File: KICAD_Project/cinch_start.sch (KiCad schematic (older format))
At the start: 30 parts, among them P101 CONN_1, P102 CONN_1, P103 CONN_1, P104 CONN_1, P105 CONN_1, P106 CONN_1, P107 CONN_1, P108 CONN_1, P109 CONN_1, P110 CONN_1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

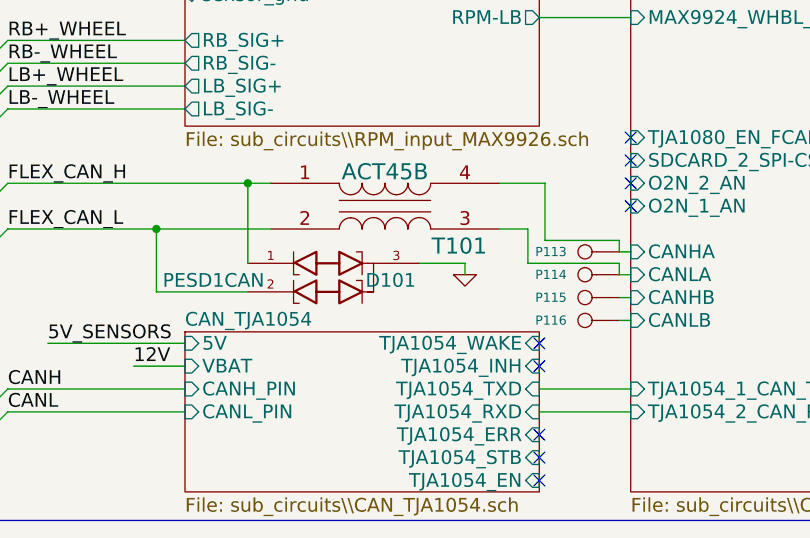
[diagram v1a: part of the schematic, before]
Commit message: updated harness pin out per layout preferences
Signed-off-by: Jared Harvey <TortiseGIT@jaredharvey.com>
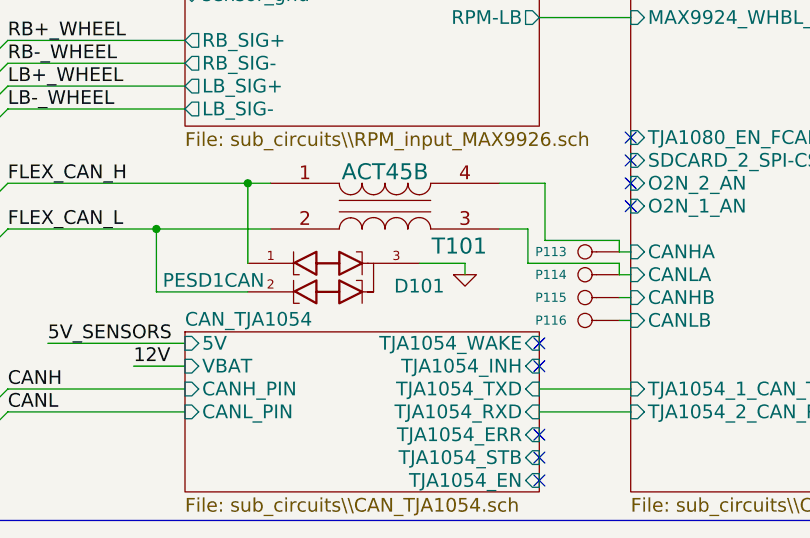
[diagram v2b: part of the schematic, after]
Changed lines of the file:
@@
-EESchema Schematic File Version 2  date 8/21/2011 9:23:44 AM
+EESchema Schematic File Version 2  date 8/21/2011 7:46:52 PM
 LIBS:power
 LIBS:device
@@
 U 1 1 4C2F1009
 P 8500 15250
-F 0 "D101" H 8775 15175 60  0000 C CNN
+F 0 "D101" H 8900 15150 60  0000 C CNN
 F 1 "PESD1CAN" H 8000 15175 60  0000 C CNN
 F 2 "SOT23-3" H 8500 15250 60  0001 C CNN

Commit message: Drafted new stepper circuit
Signed-off-by: Jared Harvey <TortiseGIT@jaredharvey.com>
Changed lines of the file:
@@
-EESchema Schematic File Version 2  date 8/21/2011 7:46:52 PM
+EESchema Schematic File Version 2  date 8/27/2011 7:35:52 AM
 LIBS:power
 LIBS:device
@@
 Sheet 1 13
 Title "freeEMS PLUS from Cinch template "
-Date "21 aug 2011"
+Date "27 aug 2011"
 Rev "A-DRAF"
 Comp "diyefi.org/openecu.info"
@@
 Wire Wire Line
 	9500 1200 9375 1200
-Connection ~ 12925 9525
 Wire Wire Line
 	13075 11525 12925 11525
 Connection ~ 12875 8075
-Wire Wire Line
-	12875 9625 13075 9625
 Connection ~ 12975 7875
-Wire Wire Line
-	12975 9425 13075 9425
 Wire Wire Line
 	12700 9325 13075 9325
@@
 Wire Wire Line
 	12700 9725 13075 9725
-Wire Wire Line
-	12925 9525 13075 9525
 Connection ~ 12925 7975
 Wire Wire Line
 	13075 11425 12975 11425
-Connection ~ 12975 9425
 Wire Wire Line
 	12875 11625 13075 11625
-Connection ~ 12875 9625
 Wire Wire Line
 	9500 1300 9375 1300
@@
 S 13075 9275 1300 800
 U 4C0F6CBF
-F0 "stepper_mc33879" 60
-F1 "sub_circuits\\stepper_mc33879.sch" 60
+F0 "stepper_L297" 60
+F1 "sub_circuits\\stepper_L297.sch" 60
 F2 "5V" I R 14375 9325 60
-F3 "879_CS" I L 13075 9325 60
-F4 "879_MOSI" I L 13075 9525 60
-F5 "879_MISO" I L 13075 9625 60
-F6 "879_SCLK" I L 13075 9425 60
-F7 "879_EN" I L 13075 9725 60
-F8 "VBAT" I R 14375 9425 60
-F9 "879_IN6" I L 13075 9925 60
-F10 "879_IN5" I L 13075 9825 60
-F11 "D5_PIN" I R 14375 9825 60
-F12 "S4_PIN" I R 14375 9925 60
-F13 "S1_PIN" I R 14375 10025 60
-F14 "D8_PIN" I R 14375 9725 60
-F15 "GND_MC33879" I R 14375 9625 60
+F3 "VBAT" I R 14375 9425 60
+F4 "OUT4" I R 14375 9725 60
+F5 "GND_L297" I R 14375 9625 60
+F6 "OUT3" I R 14375 9825 60
+F7 "OUT2" I R 14375 9925 60
+F8 "OUT1" I R 14375 10025 60
+F9 "L297_CCW" I L 13075 9725 60
+F10 "L297_CLK" I L 13075 9825 60
+F11 "L297_EN" I L 13075 9925 60
 $EndSheet
 $Sheet

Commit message: updates to the stepper
Signed-off-by: Jared Harvey <TortiseGIT@jaredharvey.com>
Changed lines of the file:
@@
-EESchema Schematic File Version 2  date 8/27/2011 7:35:52 AM
+EESchema Schematic File Version 2  date 8/27/2011 10:55:17 AM
 LIBS:power
 LIBS:device
@@
 F10 "L297_CLK" I L 13075 9825 60
 F11 "L297_EN" I L 13075 9925 60
+F12 "L297_VREF" I L 13075 9325 60
 $EndSheet
 $Sheet
